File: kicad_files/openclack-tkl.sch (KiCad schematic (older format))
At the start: 204 parts, among them CON1 USB-MINI-B, Q1 60V 1.2A, SW0:0 ESC, SW0:10 F9, SW0:11 F10, SW0:12 F11, SW0:13 F12, SW0:14 PRINT, SW0:15 SCROLL LOCK, SW0:2 F1, SW0:3 F2, SW0:4 F3, SW0:5 F4, SW0:6 F5, SW0:7 F6, SW0:8 F7, SW0:9 F8, SW1:0 `, SW1:1 1, SW1:10 0, SW1:11 -, SW1:12 =, SW1:13 BACK SPACE, SW1:14 INSERT, SW1:15 HOME, SW1:2 2, SW1:3 3, SW1:4 4, SW1:5 5, SW1:6 6, SW1:7 7, SW1:8 8, SW1:9 9, SW2:0 TAB, SW2:1 Q, SW2:10 P, SW2:11 [, SW2:12 ], SW2:13 \\, SW2:14 DELETE, SW2:15 END, SW2:2 W, SW2:3 E, SW2:4 R, SW2:5 T, SW2:6 Y, SW2:7 U, SW2:8 I, SW2:9 O, SW3:0 CAPS LOCK, SW3:1 A, SW3:10 ;, SW3:11 ', SW3:13 ENTER, SW3:14 PAGE UP, SW3:15 PAUSE, SW3:2 S, SW3:3 D, SW3:4 F, SW3:5 G, SW3:6 H, SW3:7 J, SW3:8 K, SW3:9 L, SW4:0 LEFT SHIFT, SW4:1 Z, SW4:10 /, SW4:13 RIGHT SHIFT, SW4:14 PAGE DOWN, SW4:15 UP, SW4:2 X, SW4:3 C, SW4:4 V, SW4:5 B, SW4:6 N, SW4:7 M, SW4:8 ,, SW4:9 ., SW5:0 LEFT CTRL, SW5:1 LEFT WINDOWS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

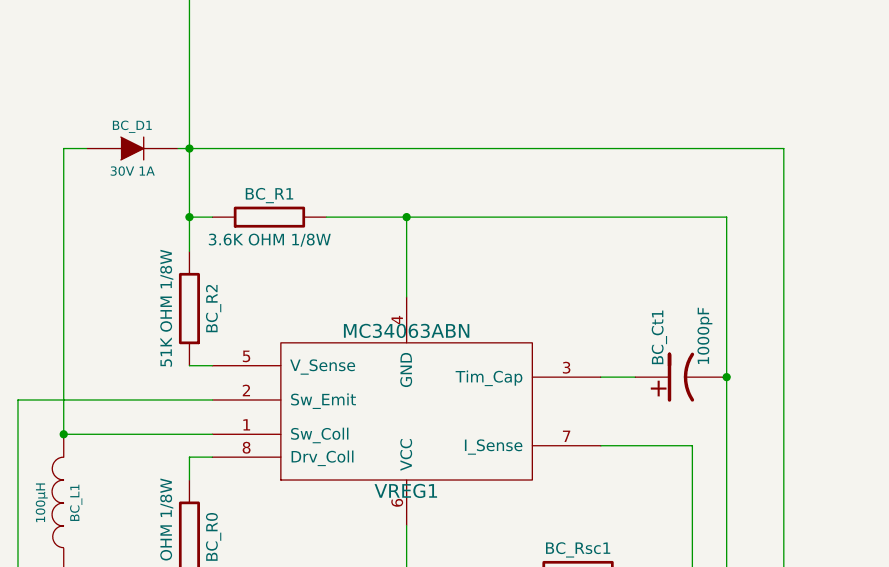
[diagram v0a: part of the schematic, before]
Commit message: Fixed error with boost converter wiring for BC_R1 found in prototype.
On the prototype this is an easy fix, basically you can just rotate the
resistor to the side and solder it to the same pin the trace goes to in
the diagram now.
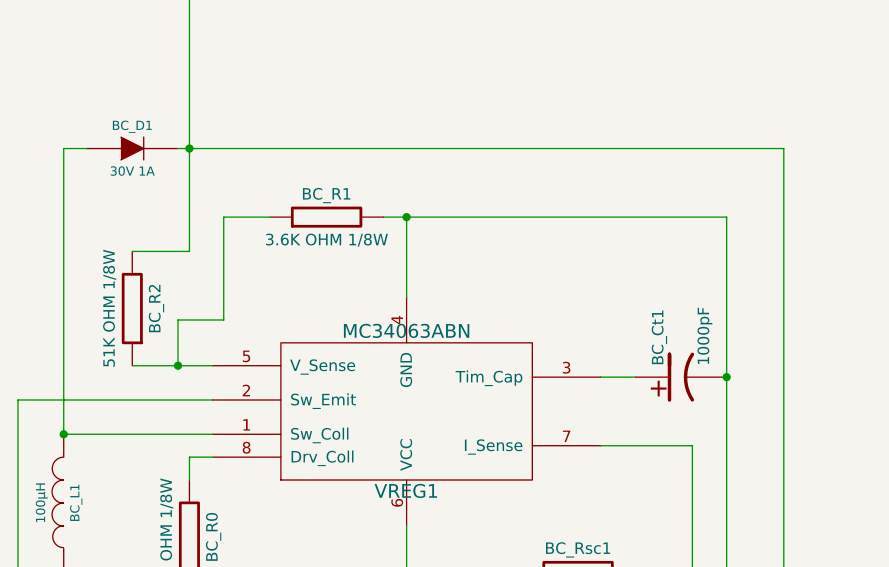
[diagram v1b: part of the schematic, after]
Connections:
- net LEDCOL0: no longer BC_R1.1
- net at BC_R2.1, VREG1.5 (V_Sense): now also BC_R1.1
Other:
- moved on the sheet: BC_R1, BC_R2
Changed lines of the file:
@@
-EESchema Schematic File Version 2  date 14/07/2013 10:01:23 PM
+EESchema Schematic File Version 2
 LIBS:components
 LIBS:openclack-tkl-cache
@@
 Sheet 1 1
 Title "Toasty TKL"
-Date "12 jul 2013"
+Date "25 jul 2013"
 Rev "REV 1A"
 Comp ""
@@
 L RESISTOR BC_R2
 U 1 1 51BE5B6D
-P -2600 8350
-F 0 "BC_R2" V -2700 8350 50  0000 C CNN
-F 1 "51K OHM 1/8W" V -2500 8350 50  0000 C CNN
-F 2 "~" H -2600 8350 60  0000 C CNN
-F 3 "~" H -2600 8350 60  0000 C CNN
-	1    -2600 8350
+P -2850 8350
+F 0 "BC_R2" V -2950 8350 50  0000 C CNN
+F 1 "51K OHM 1/8W" V -2750 8350 50  0000 C CNN
+F 2 "~" H -2850 8350 60  0000 C CNN
+F 3 "~" H -2850 8350 60  0000 C CNN
+	1    -2850 8350
 	-1   0    0    1
 $EndComp
@@
 L RESISTOR BC_R1
 U 1 1 51BE5B7C
-P -2250 7950
-F 0 "BC_R1" V -2150 7950 50  0000 C CNN
-F 1 "3.6K OHM 1/8W" V -2350 7950 50  0000 C CNN
-F 2 "~" H -2250 7950 60  0000 C CNN
-F 3 "~" H -2250 7950 60  0000 C CNN
-	1    -2250 7950
+P -2000 7950
+F 0 "BC_R1" V -1900 7950 50  0000 C CNN
+F 1 "3.6K OHM 1/8W" V -2100 7950 50  0000 C CNN
+F 2 "~" H -2000 7950 60  0000 C CNN
+F 3 "~" H -2000 7950 60  0000 C CNN
+	1    -2000 7950
 	0    -1   -1   0
 $EndComp
@@
 	1    0    0    -1
 $EndComp
+Text Label 17600 8000 2    60   ~ 0
+Q1
 Wire Wire Line
 	5850 5300 8650 5300
@@
 	-2650 7650 0    7650
 Connection ~ -1650 7950
-Wire Wire Line
-	-2600 7950 -2500 7950
 Connection ~ -1650 11200
 Wire Wire Line
-	-2000 7950 -250 7950
-Wire Wire Line
 	0    11000 0    14150
 Wire Wire Line
@@
 Wire Wire Line
 	-2600 6050 -2600 8100
-Connection ~ -2600 7950
 Connection ~ -2600 7650
 Wire Wire Line
 	11700 6050 -2600 6050
 Wire Wire Line
-	-2500 8600 -2600 8600
+	-2850 8600 -2500 8600
 Wire Wire Line
 	-3150 7650 -3050 7650
@@
 Wire Wire Line
 	22700 8400 20300 8400
-Text Label 17600 8000 2    60   ~ 0
-Q1
 Wire Wire Line
 	7650 11800 22000 11800
@@
 	9850 -4350 17000 -4350
 Connection ~ 6850 2450
+Wire Wire Line
+	-250 7950 -1750 7950
+Wire Wire Line
+	-2600 8100 -2850 8100
+Wire Wire Line
+	-2250 7950 -2450 7950
+Wire Wire Line
+	-2450 7950 -2450 8400
+Wire Wire Line
+	-2450 8400 -2650 8400
+Wire Wire Line
+	-2650 8400 -2650 8600
+Connection ~ -2650 8600
 $EndSCHEMATC
